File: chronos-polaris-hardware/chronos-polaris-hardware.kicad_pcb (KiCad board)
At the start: 2 copper layers, 35 x 50 mm, 55 parts, among them J1 Conn_01x03_Pin, J2 Conn_01x03_Pin, J3 Conn_01x03_Pin, J4 Conn_01x03_Pin, J5 Conn_01x03_Pin, J6 Conn_01x04, J7 Conn_01x04, J8 Conn_01x02, P1 WJ124-3_81-6P, U1 TPS62172DSGR, U10 MSK12C02-HB, U11 SS54_C22452, U12 AP20P30Q, U13 DMP2200UDW-7, U14 FC-B1010RGBT-HG, U15 TYPE-C_14PLC-H10_0, U2 ESP32-S2-SOLO-2-N4, U3 BMI088, U4 BMP280, U5 TF_PUSH, U6 LM2596S-5_0, U7 AP20P30Q, U8 2N7002KDW_72K, U9 SS-12D10L3

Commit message: finish PCB layout
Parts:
- removed R7: 10k, Resistor_SMD:R_0603_1608Metric
- removed U13: DMP2200UDW-7, polaris-fp:SOT-363_L2.0-W1.3-P0.65-LS2.1-BL
- added R14: 30k, Resistor_SMD:R_0603_1608Metric, B.Cu at (113.8, 101.6)
- added R15: 10k, Resistor_SMD:R_0603_1608Metric, B.Cu at (110.2, 101.6)
- added R16: 10k, Resistor_SMD:R_0603_1608Metric, B.Cu at (128.2, 101.6)
- added R17: 30k, Resistor_SMD:R_0603_1608Metric, B.Cu at (124.6, 101.4)
- added R18: 10k, Resistor_SMD:R_0603_1608Metric, B.Cu at (121.0, 101.6)
- C1, C10, C2, C5, C6, C7, C8, C9, D1, L1, R1, R12, R13, R2, R3, R5, R6, R8, U1, U11, U12, U2, U3, U4, U5, U7, U8: moved to B.Cu
- moved H3 137.9 mm to (103.6, 146.4)
- moved H1 123.6 mm to (103.6, 103.6)
- moved H2 111.1 mm to (134.4, 146.4)
- moved R8 101.7 mm to (108.4, 144.2), turned to 180 degrees
- moved C5 99.7 mm to (109.4, 146.0), turned to 90 degrees
- moved H4 96.7 mm to (134.4, 103.6)
- moved R4 92.8 mm to (110.2, 109.6), turned to 90 degrees
- moved BUZ1 90.5 mm to (104.5, 111.1)
- moved C9 90.1 mm to (119.2, 116.6), turned to 180 degrees
- moved R6 87.8 mm to (117.4, 101.4), turned to 180 degrees
- moved C7 86.2 mm to (121.5, 123.9), turned to 90 degrees
- moved R3 86.1 mm to (114.6, 106.2)
- moved C6 84.6 mm to (122.9, 123.9), turned to 90 degrees
- moved C8 84.5 mm to (125.2, 113.6), turned to -90 degrees
- moved R9 84.1 mm to (125.2, 141.2)
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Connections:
- R10 pad 2: Net-(U2-IO11) -> Net-(U2-RXD0)
- R11 pad 2: Net-(U2-IO12) -> Net-(U2-TXD0)
- R9 pad 2: Net-(U2-IO10) -> Net-(U2-IO42)
- U2 pad 17: unconnected-(U2-IO9-Pad17) -> Net-(U2-IO9)
- U2 pad 34: Net-(U2-IO41) -> unconnected-(U2-IO41-Pad34)
- U5 pad 2: Net-(U2-TXD0) -> Net-(U2-IO12)
- U5 pad 3: Net-(U2-RXD0) -> Net-(U2-IO11)
- U5 pad 5: Net-(U2-IO42) -> Net-(U2-IO10)
- U5 pad 7: Net-(U2-IO41) -> Net-(U2-IO9)
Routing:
- net GND: track 0.00 -> 293.2 mm, vias 0 -> 35
- net 3.3V: track 0.00 -> 203.0 mm, vias 0 -> 15
- net /MAIN CTRL: track 0.00 -> 88.1 mm, vias 0 -> 4
- net 5V: track 0.00 -> 86.0 mm
- net /DROGUE DETECT: track 0.00 -> 71.0 mm, vias 0 -> 4
- net /MAIN DETECT: track 0.00 -> 60.1 mm
- net /DROGUE CTRL: track 0.00 -> 59.4 mm, vias 0 -> 4
- net /BAT+: track 0.00 -> 57.0 mm
- net /MOSI / SDI: track 0.00 -> 53.3 mm, vias 0 -> 3
- net /RESET: track 0.00 -> 46.0 mm, vias 0 -> 3
- net /MISO / SDO: track 0.00 -> 45.2 mm, vias 0 -> 2
- net /SPI CLK: track 0.00 -> 39.0 mm, vias 0 -> 2
- net Net-(U11-K): track 0.00 -> 34.5 mm, vias 0 -> 1
- net Net-(U2-IO20): track 0.00 -> 34.1 mm, vias 0 -> 1
- net Net-(U2-IO19): track 0.00 -> 32.4 mm, vias 0 -> 1
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- added copper zone on B.Cu, net /BAT+
- added copper zone on B.Cu, net GND
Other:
- board size 35 x 50 mm -> 38 x 50 mm

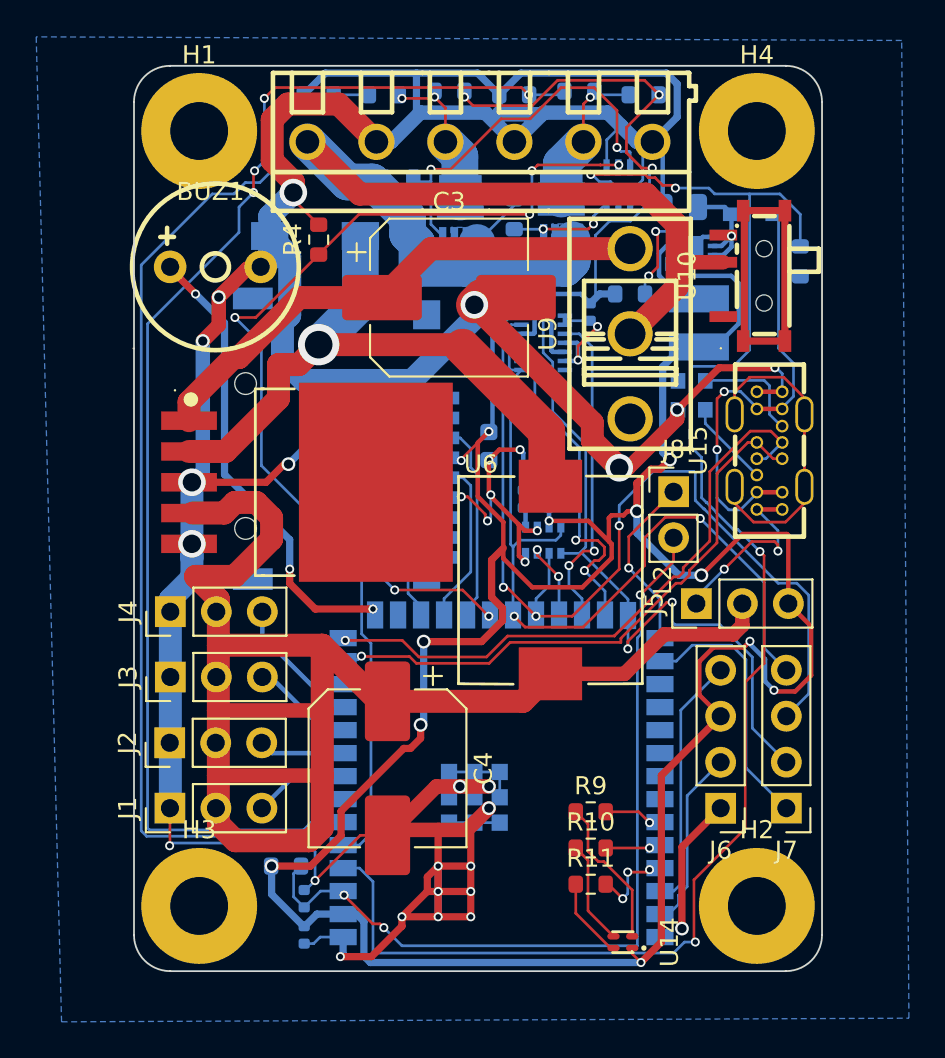
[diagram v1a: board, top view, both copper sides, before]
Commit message: improve ground planes
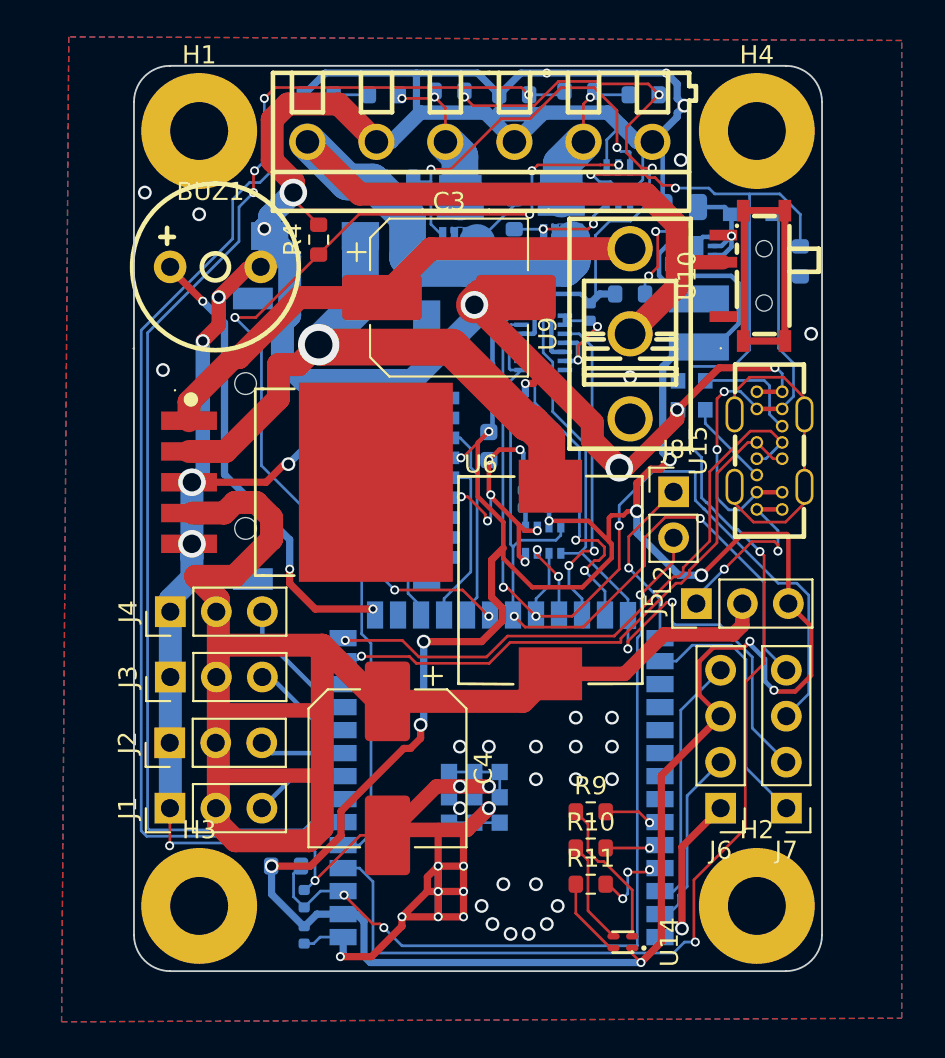
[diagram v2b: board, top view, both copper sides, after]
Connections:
- H2 pad 1: (no net) -> GND
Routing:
- net GND: track 293.2 -> 294.5 mm, vias 35 -> 65
- net /MAIN DETECT: track 60.1 -> 59.2 mm
- added copper zone on F.Cu, net GND

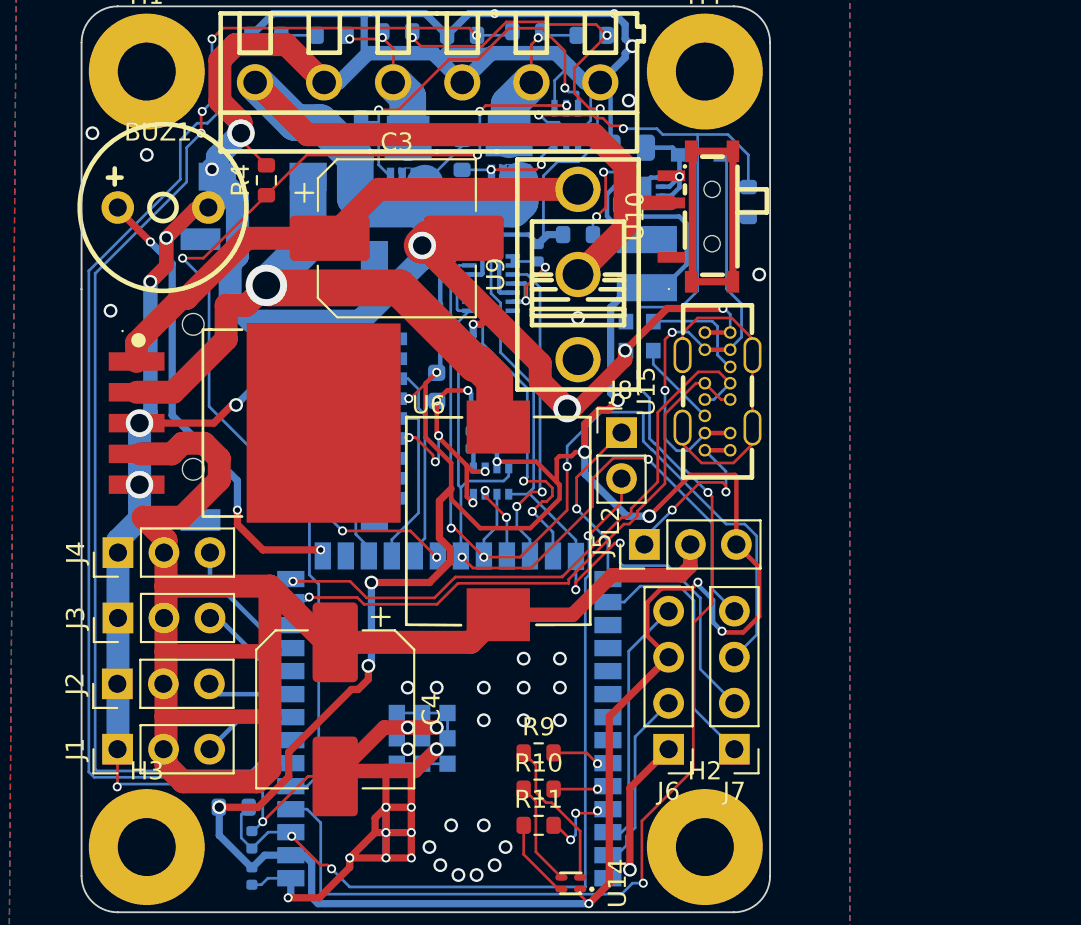
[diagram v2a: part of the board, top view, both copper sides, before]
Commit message: switch to compact 5v regulator
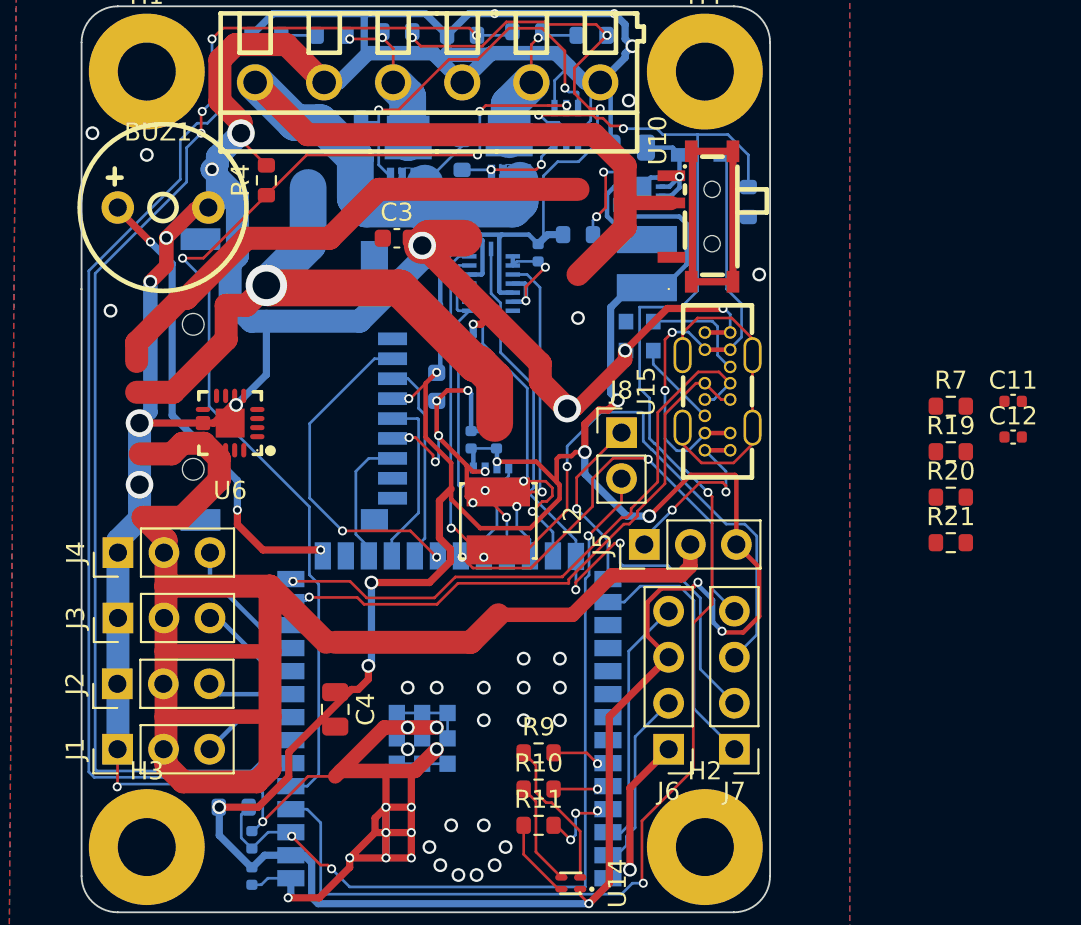
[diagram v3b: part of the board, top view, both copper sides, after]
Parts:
- removed U11: SS54_C22452, polaris-fp:SMA_L4.4-W2.8-LS5.4-R-RD
- removed U9: SS-12D10L3, polaris-fp:SW-TH_SS-12D10L3
- added C11: 3.3nF, Capacitor_SMD:C_0402_1005Metric, F.Cu at (151.4, 121.8)
- added C12: 100nF, Capacitor_SMD:C_0402_1005Metric, F.Cu at (151.4, 123.8)
- added R19: 100k, Resistor_SMD:R_0603_1608Metric, F.Cu at (148.0, 124.6)
- added R20: 160k, Resistor_SMD:R_0603_1608Metric, F.Cu at (148.0, 127.1)
- added R21: 10k, Resistor_SMD:R_0603_1608Metric, F.Cu at (148.0, 129.6)
- added R7: 30k, Resistor_SMD:R_0603_1608Metric, F.Cu at (148.0, 122.1)
- C3: value 220uF -> 22uF; footprint Capacitor_SMD:CP_Elec_8x10.5 -> Capacitor_SMD:C_0603_1608Metric
- C4: value 220uF -> 10uF; footprint Capacitor_SMD:CP_Elec_8x10.5 -> Capacitor_SMD:C_0805_2012Metric
- L2: value 33uH -> 2.2uH; footprint polaris-fp:IND-SMD_L11.5-W10.0_SMMS1040 -> polaris-fp:IND-SMD_L4.0-W4.0
- U6: value LM2596S-5_0 -> TLV62130RGTR; footprint polaris-fp:TO-263-5_L10.2-W8.9-P1.70-BR -> polaris-fp:QFN-16_L3.0-W3.0-P0.50-TL-EP
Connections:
- C3 pad 1: Net-(U6-VIN) -> 5V
- C4 pad 1: 5V -> /BAT+
- L2 pad 1: Net-(U11-K) -> 5V
- L2 pad 2: 5V -> Net-(L2-Pad2)
- U2 pad 33: unconnected-(U2-IO40-Pad33) -> 5V_ENABLE
- U2 pad 34: unconnected-(U2-IO41-Pad34) -> 5V_5%BOOST
- U6 pad 1: Net-(U6-VIN) -> Net-(L2-Pad2)
- U6 pad 2: Net-(U11-K) -> Net-(L2-Pad2)
- U6 pad 3: GND -> Net-(L2-Pad2)
- U6 pad 4: 5V -> Net-(U6-PG)
- U6 pad 5: GND -> Net-(U6-FB)
- U6 pad 6: unconnected-(U6-EP-Pad6) -> GND

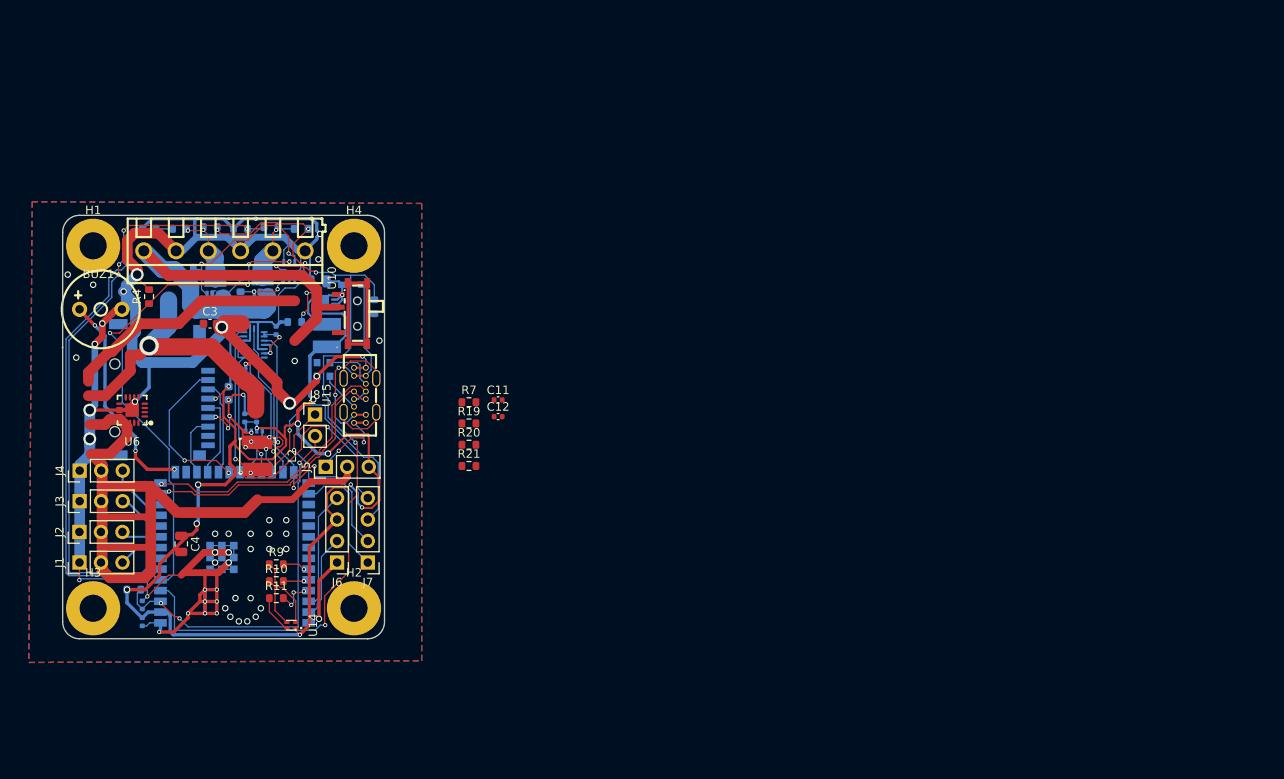
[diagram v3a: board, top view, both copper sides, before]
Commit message: fix V in switching with usb, remove diode
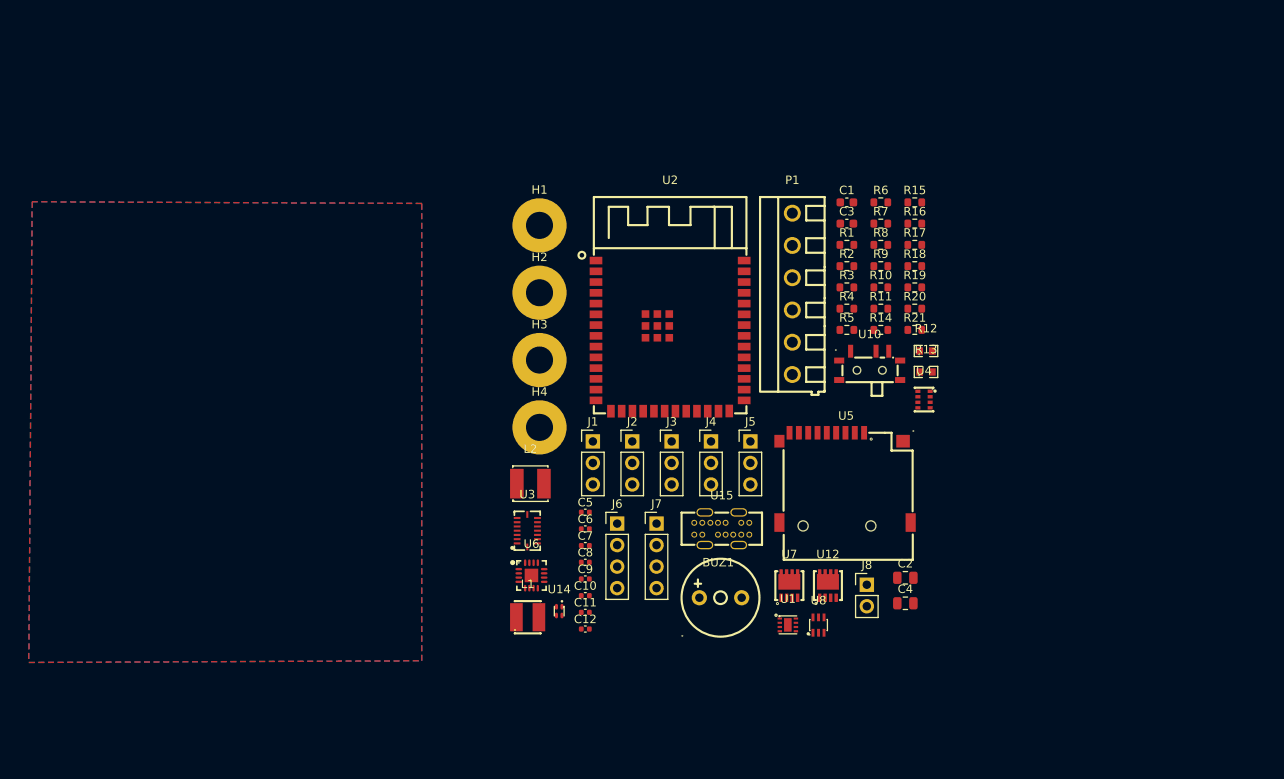
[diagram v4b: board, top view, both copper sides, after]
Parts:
- removed D1: 1N5819WS, polaris-fp:SOD-323_L1.8-W1.3-LS2.5-RD
- C1, C10, C2, C5, C6, C7, C8, C9, L1, R1, R12, R13, R14, R15, R16, R17, R18, R2, R3, R5, R6, R8, U1, U12, U2, U3, U4, U5, U7, U8: moved to F.Cu
- moved R8 97.1 mm to (196.6, 103.5), turned to 0 degrees
- moved R15 90.5 mm to (200.6, 98.5), turned to 0 degrees
- moved C4 85.8 mm to (199.5, 145.8), turned to 0 degrees
- moved R14 83.7 mm to (196.6, 113.5), turned to 0 degrees
- moved R4 82.4 mm to (192.6, 111.0), turned to 0 degrees
- moved U5 81.2 mm to (192.4, 131.0), turned to 0 degrees
- moved BUZ1 80.7 mm to (177.7, 145.2)
- moved U12 80.7 mm to (190.4, 143.7), turned to 0 degrees
- moved R18 79.7 mm to (200.6, 106.0), turned to 0 degrees
- moved R9 79.6 mm to (196.6, 106.0)
- moved R10 79.4 mm to (196.6, 108.5)
- moved R6 79.2 mm to (196.6, 98.5), turned to 0 degrees
- moved U4 79.2 mm to (201.7, 121.8), turned to 0 degrees
- moved R11 79.1 mm to (196.6, 111.0)
- moved R3 78.0 mm to (192.6, 108.5)
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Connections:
- C2 pad 1: Net-(D1-C) -> Net-(U1-EN)
- U1 pad 2: Net-(D1-C) -> Net-(U1-EN)
- U1 pad 3: Net-(D1-C) -> Net-(U1-EN)
- U10 pad 1: unconnected-(U10-Pad1) -> /BAT+
- U10 pad 2: /BAT+ -> Net-(U1-EN)
- U10 pad 3: Net-(D1-C) -> /USB_5V
- U15 pad A4: Net-(D1-A) -> /USB_5V
- U15 pad A9: Net-(D1-A) -> /USB_5V
- U15 pad B4: Net-(D1-A) -> /USB_5V
- U15 pad B9: Net-(D1-A) -> /USB_5V
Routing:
- net GND: track 294.5 -> 0.00 mm, vias 65 -> 0
- net 3.3V: track 202.8 -> 0.00 mm, vias 15 -> 0
- net /MAIN CTRL: track 88.1 -> 0.00 mm, vias 4 -> 0
- net 5V: track 86.0 -> 0.00 mm
- net /DROGUE DETECT: track 71.0 -> 0.00 mm, vias 4 -> 0
- net /DROGUE CTRL: track 59.4 -> 0.00 mm, vias 4 -> 0
- net /MAIN DETECT: track 59.2 -> 0.00 mm
- net /BAT+: track 57.0 -> 0.00 mm
- net /MOSI / SDI: track 53.3 -> 0.00 mm, vias 3 -> 0
- net /RESET: track 46.0 -> 0.00 mm, vias 3 -> 0
- net /MISO / SDO: track 45.2 -> 0.00 mm, vias 2 -> 0
- net /SPI CLK: track 39.0 -> 0.00 mm, vias 2 -> 0
- net Net-(U11-K): track 34.2 -> 0.00 mm, vias 1 -> 0
- net Net-(U2-IO20): track 34.1 -> 0.00 mm, vias 1 -> 0
- net Net-(U2-IO19): track 32.4 -> 0.00 mm, vias 1 -> 0
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- removed copper zone on B.Cu, net /BAT+
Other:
- board outline removed
